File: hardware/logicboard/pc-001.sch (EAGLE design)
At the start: 5 parts, among them J4 DNP, J5 DNP

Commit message: New Pineapple Logo was put on the board.
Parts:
- added LOGO1: OSHW-LOGOS, SparkFun-Aesthetics:OSHW-LOGOS
- added U$1: PINEAPPLELOGO2SILKMINI, pineapplelogo:PINEAPPLELOGO2SILKMINI

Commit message: 14p Analog input.
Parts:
- ANALOG: device con-ml:ML10L -> con-ml:ML14L
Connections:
- new net A0: ANALOG.2, J4.2, RN1.5
- new net A6: J4.8, RN2.3
- net A1: now also ANALOG.4, RN1.4; no longer ANALOG.2, RN1.5
- net A2: now also ANALOG.6, RN1.3; no longer ANALOG.4, RN1.4
- net A3: now also ANALOG.8, RN1.2; no longer ANALOG.6, RN1.3
- net A4: now also ANALOG.10, RN2.5; no longer ANALOG.8, RN1.2
- net A5: now also ANALOG.12, RN2.4; no longer ANALOG.10, RN2.5
- net VCC: now also ANALOG.11, ANALOG.13
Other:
- moved on the sheet: J4, RN2

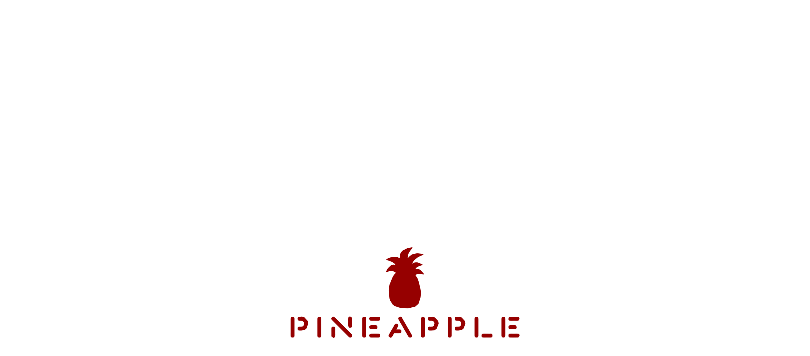
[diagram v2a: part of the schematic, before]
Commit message: Pineapple Logo (vector -> bitmap), OSHW Logo (silk -> copper).
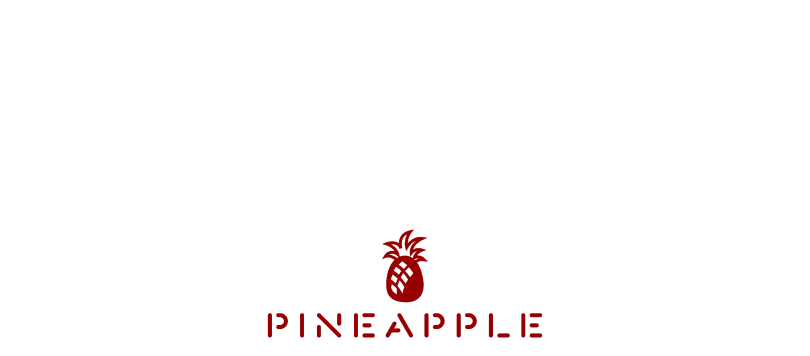
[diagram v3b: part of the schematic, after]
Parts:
- LOGO1: value OSHW-LOGOS -> OSHW-LOGOS-COPPER; device SparkFun-Aesthetics:OSHW-LOGOS -> SparkFun-Aesthetics:OSHW-LOGOS-COPPER
- U$1: value PINEAPPLELOGO2SILKMINI -> PINEAPPLE450; device pineapplelogo:PINEAPPLELOGO2SILKMINI -> pineapple:PINEAPPLE450
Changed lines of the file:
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@@
 <part name="RN2" library="resistor-net" library_urn="urn:adsk.eagle:library:343" deviceset="RN04" device="" package3d_urn="urn:adsk.eagle:package:24976/1" value="10k"/>
 <part name="FRAME1" library="frames" library_urn="urn:adsk.eagle:library:229" deviceset="A4L-LOC" device=""/>
-<part name="LOGO1" library="SparkFun-Aesthetics" library_urn="urn:adsk.eagle:library:507" deviceset="OSHW-LOGO" device="S" package3d_urn="urn:adsk.eagle:package:37099/1"/>
-<part name="U$1" library="pineapplelogo" deviceset="PINEAPPLELOGO2SILKMINI" device=""/>
+<part name="LOGO1" library="SparkFun-Aesthetics" deviceset="OSHW-LOGO" device="S-COPPER" value="OSHW-LOGOS-COPPER"/>
+<part name="U$1" library="pineapple" deviceset="PINEAPPLE450" device=""/>
 <part name="ANALOG" library="con-ml" library_urn="urn:adsk.eagle:library:164" deviceset="ML14L" device="" package3d_urn="urn:adsk.eagle:package:8677/1"/>
 </parts>
